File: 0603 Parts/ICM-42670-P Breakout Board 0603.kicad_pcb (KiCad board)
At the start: 2 copper layers, 18 x 26.5 mm, 12 parts, among them J2 Conn_01x09_Pin, U1 ICM-42670-P, U3 MCP1700x-300xxTT

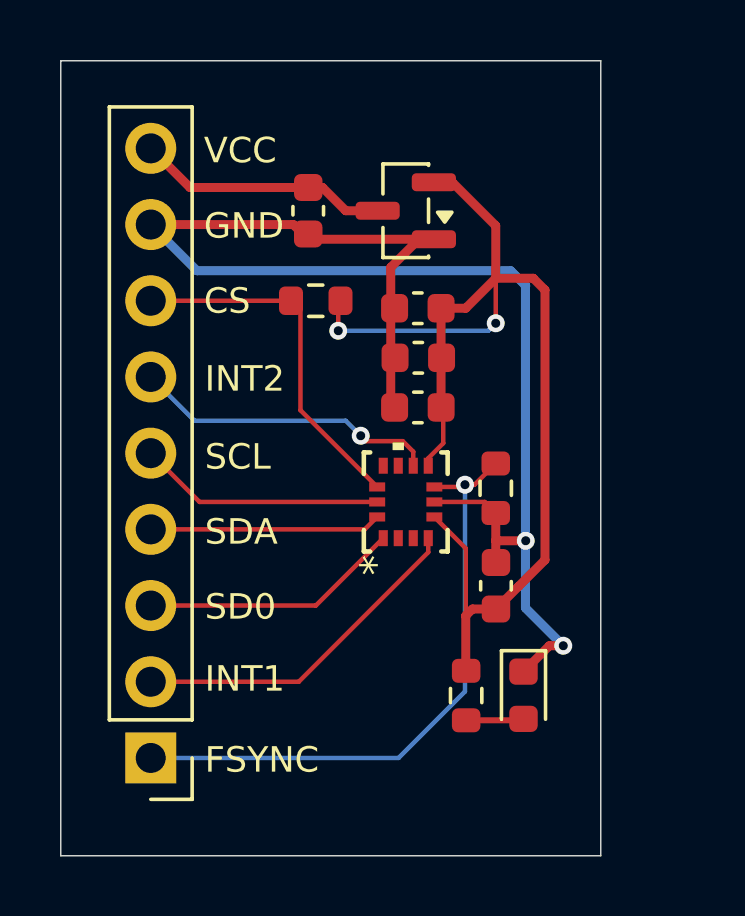
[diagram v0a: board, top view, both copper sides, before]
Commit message: Updated PCB and Schematic to include Pull Ups for SCK SDA I2c
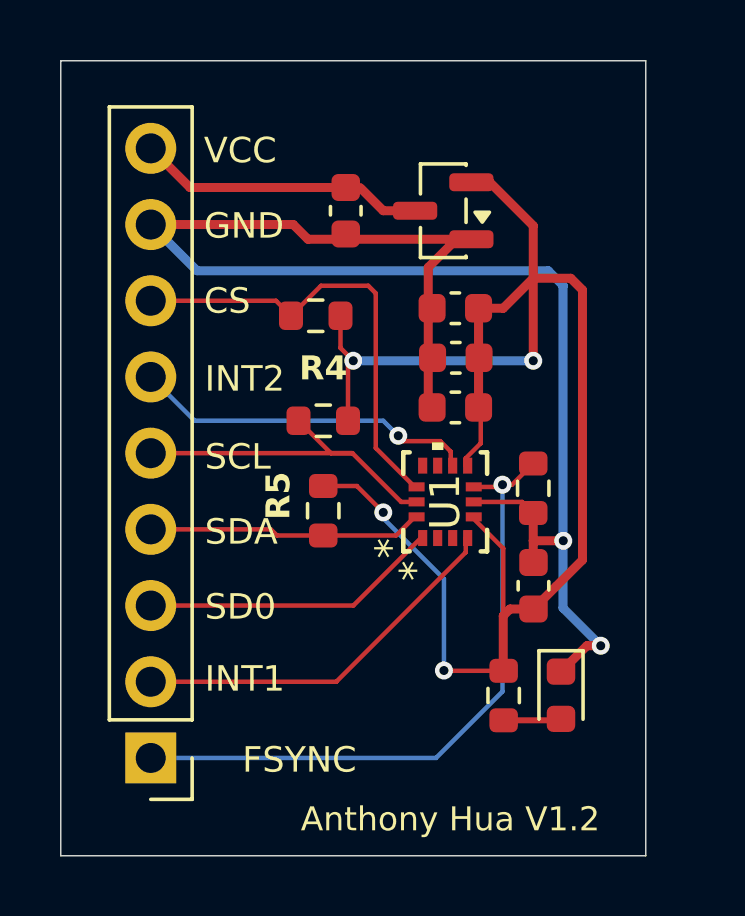
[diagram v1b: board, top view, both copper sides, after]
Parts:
- added R4: 10 kΩ, Resistor_SMD:R_0603_1608Metric, F.Cu at (64.2, 35.0)
- added R5: 10 kΩ, Resistor_SMD:R_0603_1608Metric, F.Cu at (64.2, 38.0)
- U3: value MCP1700x-300xxTT -> MCP1700x-330xxTT
- moved U1 1.31 mm to (68.3, 37.7)
- moved C1 1.25 mm to (68.7, 32.9)
- moved C2 1.25 mm to (68.7, 34.6)
- moved C3 1.25 mm to (71.3, 40.5)
- moved C4 1.25 mm to (68.7, 31.2)
- moved C5 1.25 mm to (65.0, 28.0)
- moved D1 1.25 mm to (72.2, 44.1)
- moved R2 1.25 mm to (71.2, 37.2)
- moved R3 1.25 mm to (70.3, 44.2)
- moved U3 1.25 mm to (68.2, 28.0)
- moved R1 0.50 mm to (64.0, 31.5)
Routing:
- net /3V3_Clean: track 40.6 -> 55.7 mm, vias 2 -> 4
- net /SCL: track 8.22 -> 11.7 mm
- net /CS: track 12.3 -> 15.2 mm
- net GND: track 47.5 -> 50.0 mm
- net /SDA: track 7.72 -> 9.14 mm
- net /SDO: track 8.68 -> 9.93 mm
- net /INT2: track 10.3 -> 11.5 mm
- net /INT1: track 11.5 -> 12.8 mm
- net /FSYNC: track 20.7 -> 22.0 mm
- net /5V / 3V3: track 8.42 -> 9.20 mm
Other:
- board size 18 x 26.5 mm -> 19.5 x 26.5 mm
- board text added: "Anthony Hua V1.2"
